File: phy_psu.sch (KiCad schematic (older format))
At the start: 2 parts

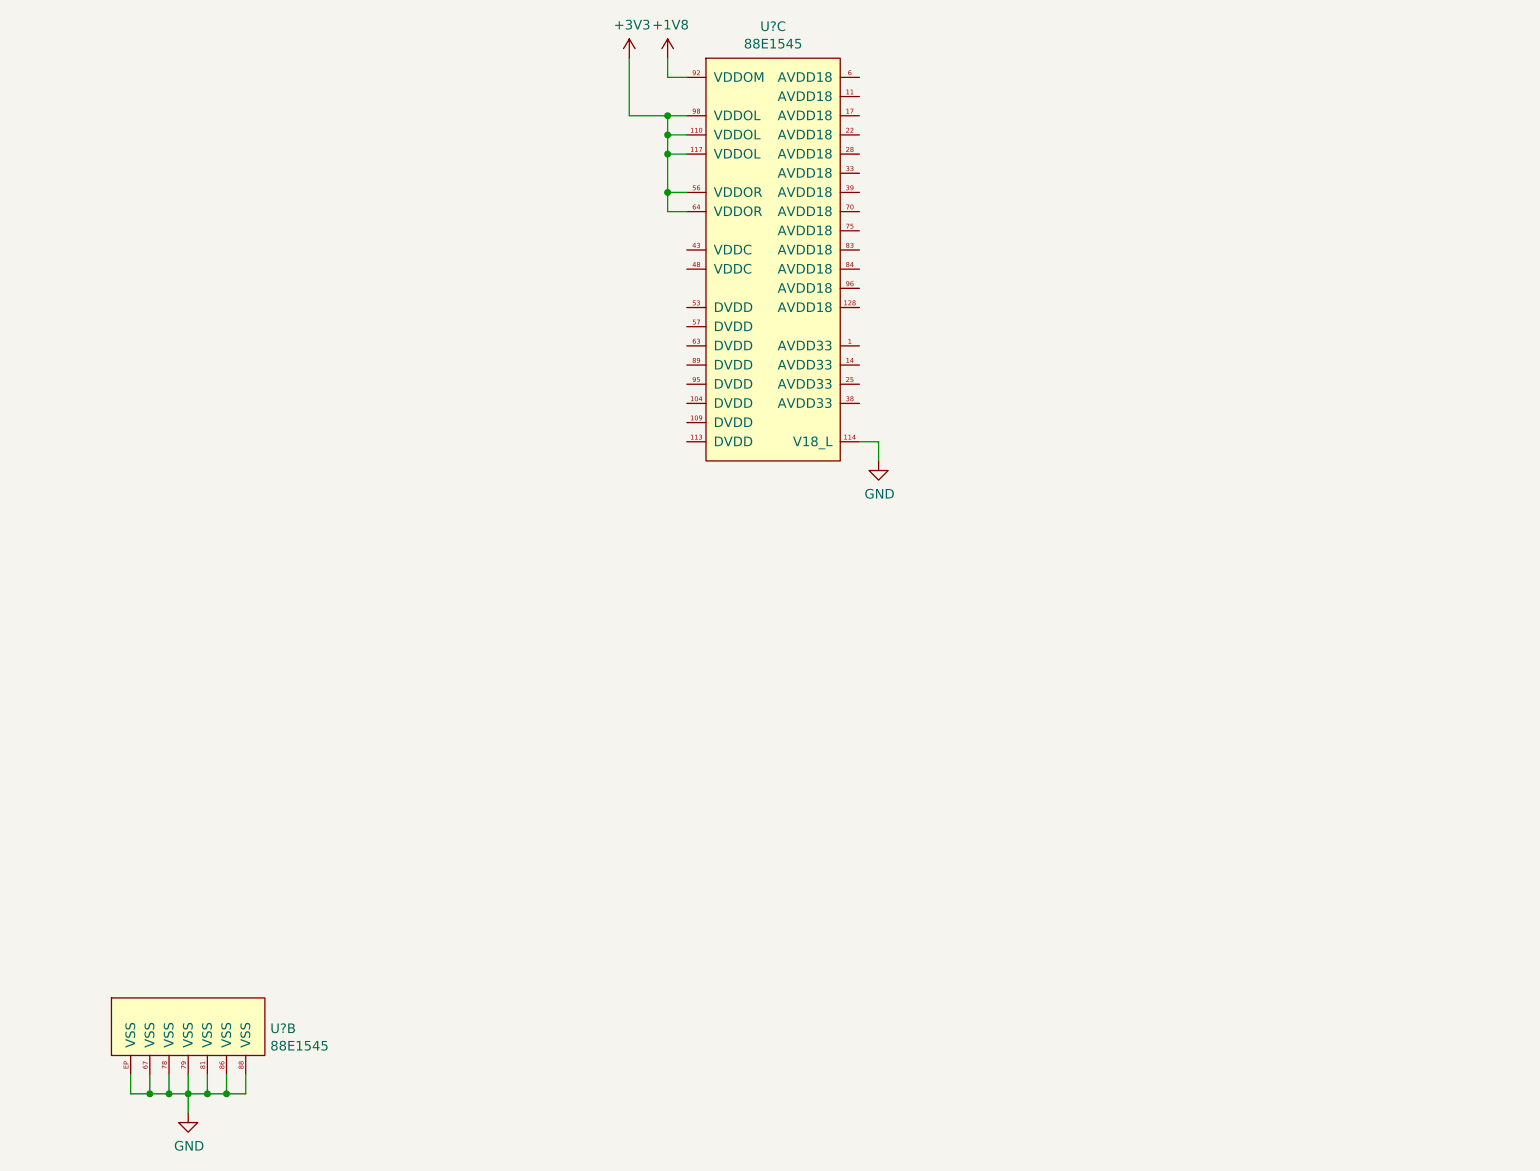
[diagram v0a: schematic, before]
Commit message: sch: Done PHY power supplies
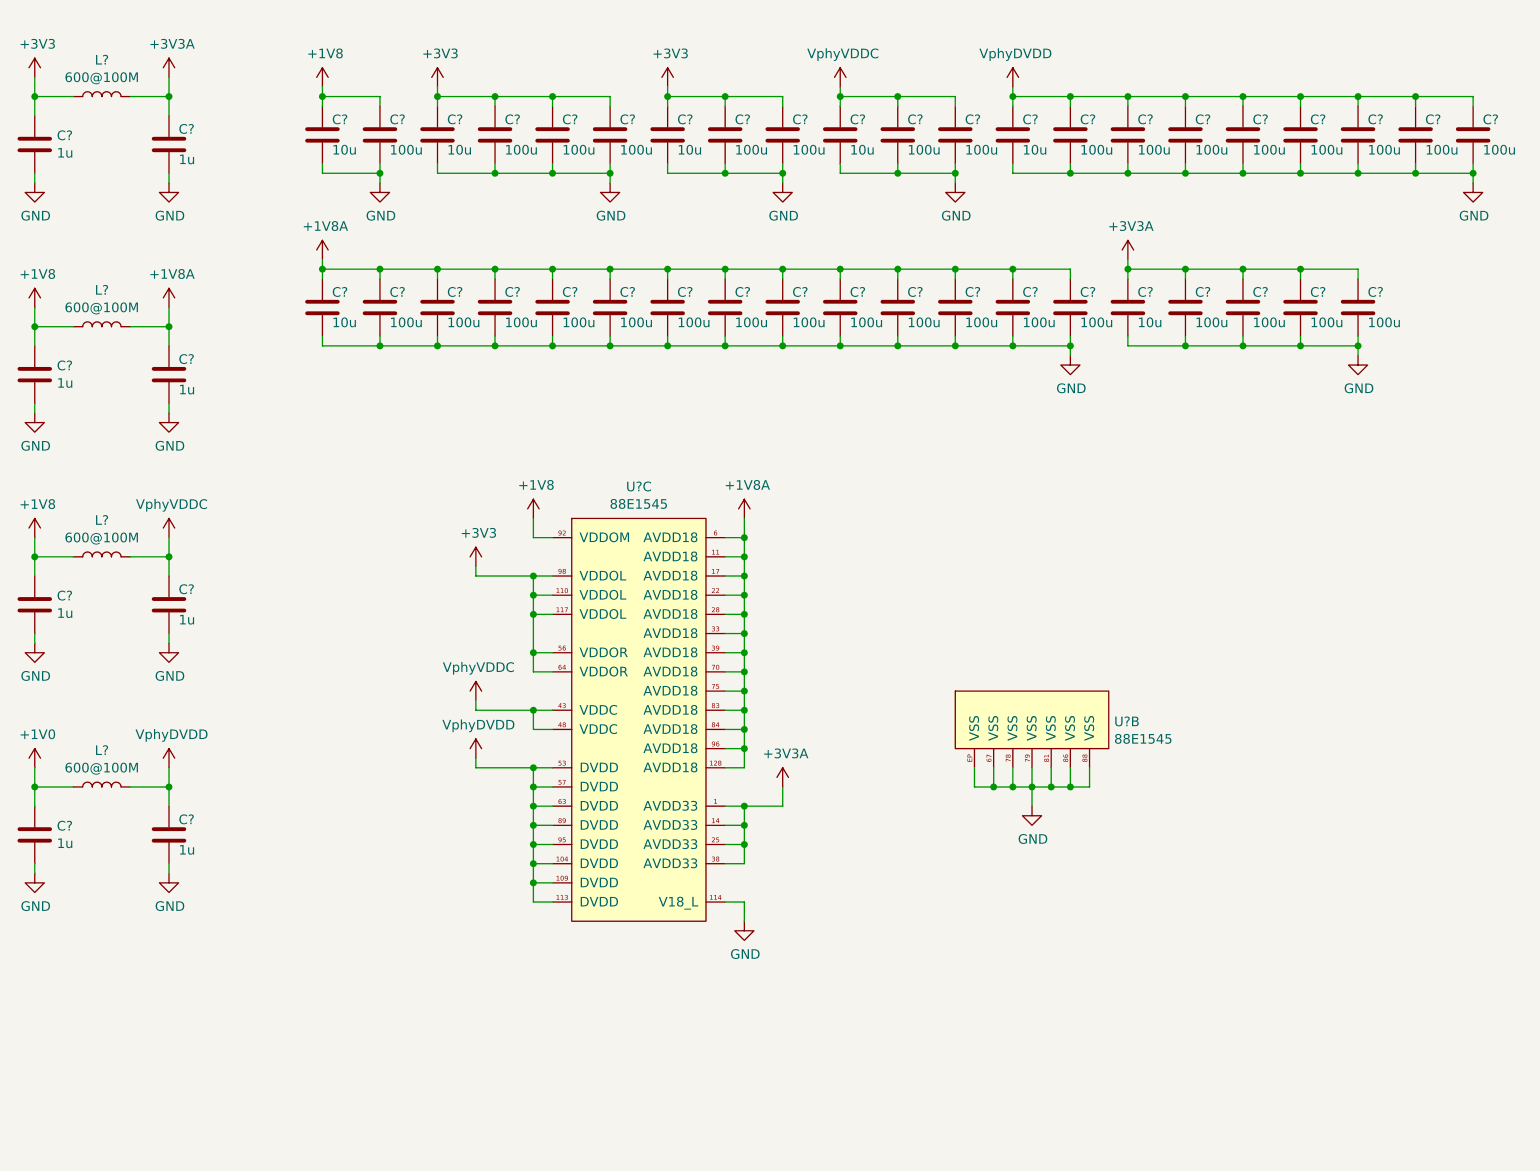
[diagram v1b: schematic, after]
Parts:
- added C? (x8): 1u, symbol Device:C
- added C? (x7): 10u, symbol Device:C
- added C? (x33): 100u, symbol Device:C
- added L? (x4): 600@100M, symbol Device:L
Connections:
- net +1V8: now also C?.1, C?.1, C?.1, C?.1, L?.1, L?.1
- net +3V3: now also C?.1, C?.1, C?.1, C?.1, C?.1, C?.1, C?.1, C?.1, L?.1
- net GND: now also C?.2, C?.2, C?.2, C?.2, C?.2, C?.2, C?.2, C?.2, C?.2, C?.2, C?.2, C?.2, C?.2, C?.2, C?.2, C?.2, C?.2, C?.2, C?.2, C?.2, C?.2, C?.2, C?.2, C?.2, C?.2, C?.2, C?.2, C?.2, C?.2, C?.2, C?.2, C?.2, C?.2, C?.2, C?.2, C?.2, C?.2, C?.2, C?.2, C?.2, C?.2, C?.2, C?.2, C?.2, C?.2, C?.2, C?.2, C?.2
- net +3V3A: now reaches U?.1 (AVDD33)
- net +3V3A: now also U?.14 (AVDD33), U?.25 (AVDD33), U?.38 (AVDD33), C?.1, C?.1, C?.1, C?.1, C?.1, C?.1, L?.2
- net VphyDVDD: now reaches U?.104 (DVDD)
- net VphyDVDD: now also U?.109 (DVDD), U?.113 (DVDD), U?.53 (DVDD), U?.57 (DVDD), U?.63 (DVDD), U?.89 (DVDD), U?.95 (DVDD), C?.1, C?.1, C?.1, C?.1, C?.1, C?.1, C?.1, C?.1, C?.1, C?.1, L?.2
- net +1V8A: now reaches U?.11 (AVDD18)
- net +1V8A: now also U?.128 (AVDD18), U?.17 (AVDD18), U?.22 (AVDD18), U?.28 (AVDD18), U?.33 (AVDD18), U?.39 (AVDD18), U?.6 (AVDD18), U?.70 (AVDD18), U?.75 (AVDD18), U?.83 (AVDD18), U?.84 (AVDD18), U?.96 (AVDD18), C?.1, C?.1, C?.1, C?.1, C?.1, C?.1, C?.1, C?.1, C?.1, C?.1, C?.1, C?.1, C?.1, C?.1, C?.1, L?.2
- net VphyVDDC: now reaches U?.43 (VDDC)
- net VphyVDDC: now also U?.48 (VDDC), C?.1, C?.1, C?.1, C?.1, L?.2
- new net +1V0: C?.1, L?.1
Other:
- moved on the sheet: U?B, U?C
